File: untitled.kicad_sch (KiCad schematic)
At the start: 4 parts

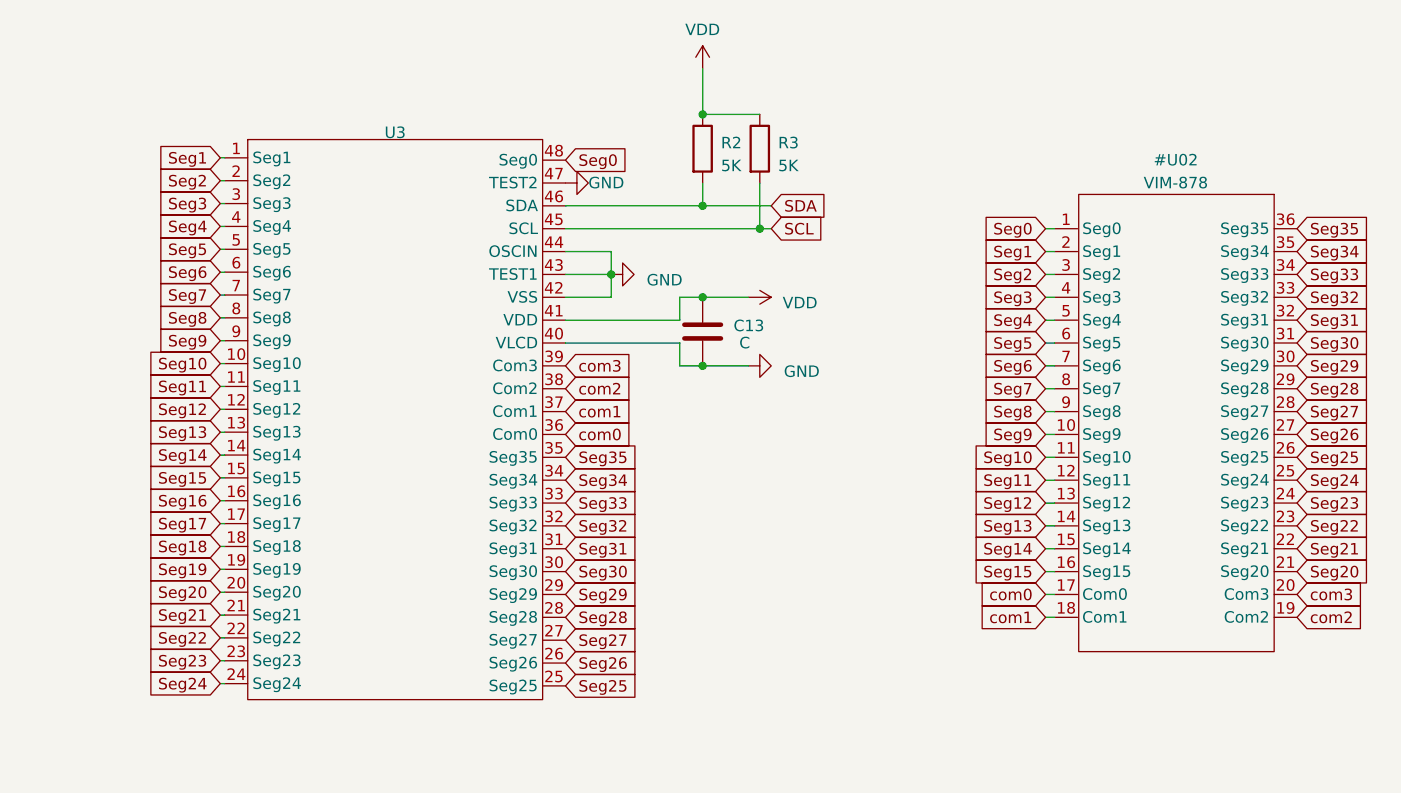
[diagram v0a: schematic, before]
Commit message: Adjusted the VDD supply schematic
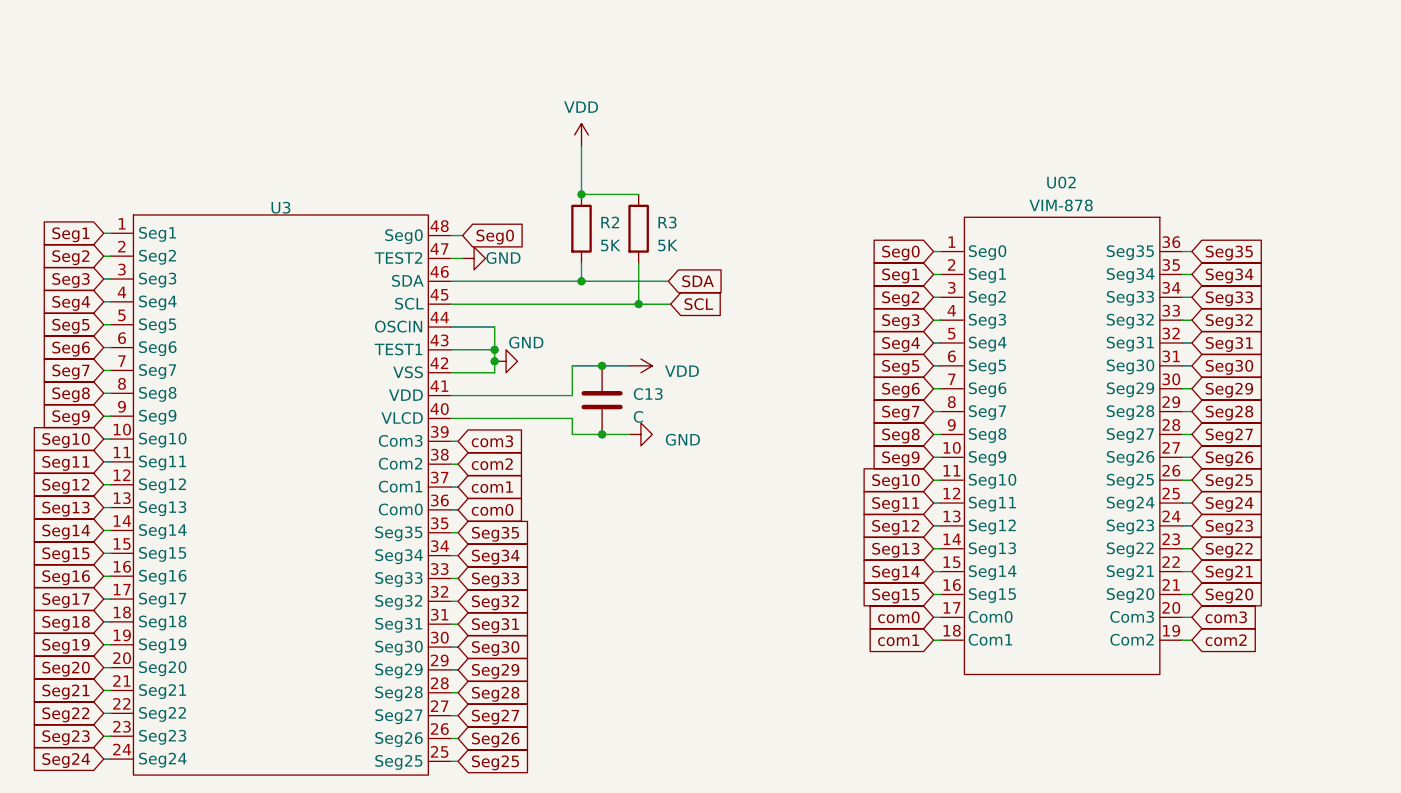
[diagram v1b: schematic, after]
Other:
- moved on the sheet: C13, R2, R3, U3
